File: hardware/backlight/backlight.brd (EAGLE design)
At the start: 58.4 x 68.2 mm, 39 parts, among them J1 1x8 header, U1 ATTINY45-20SU

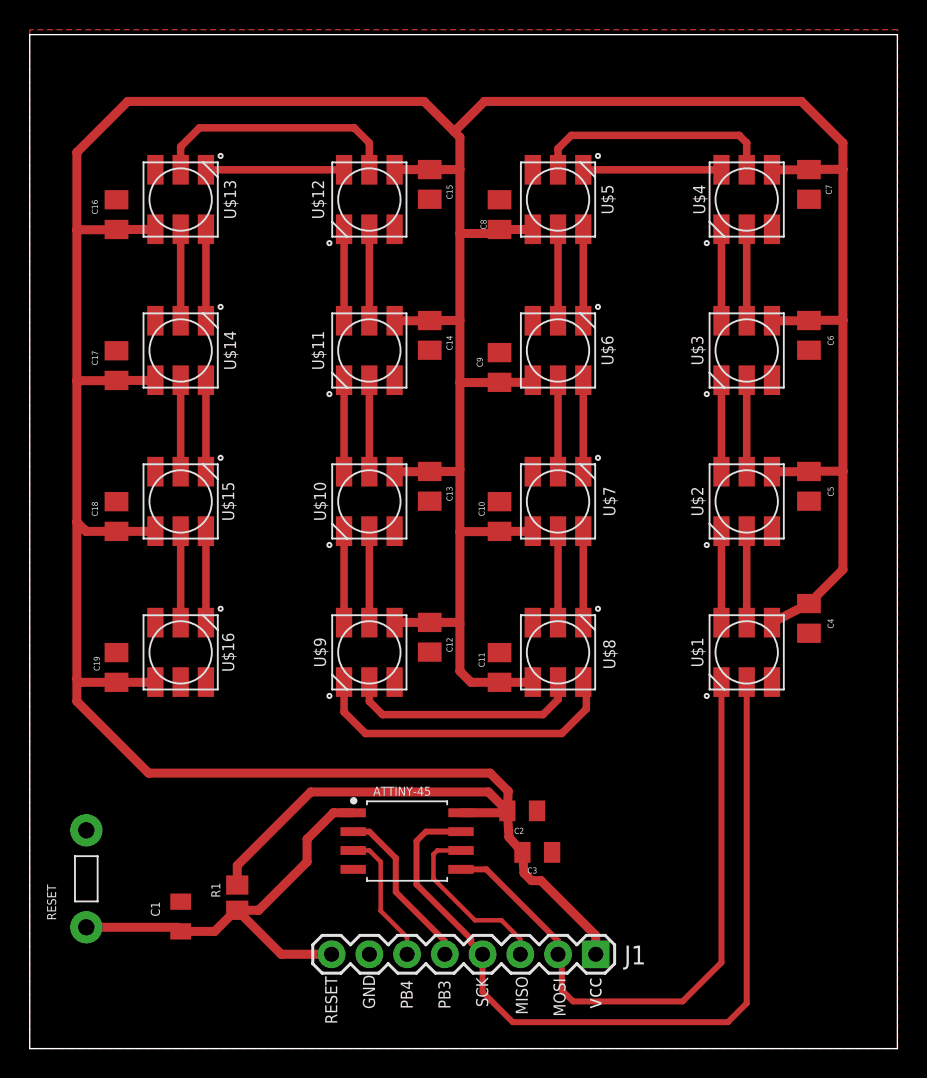
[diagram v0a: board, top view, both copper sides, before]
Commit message: thicken traces again
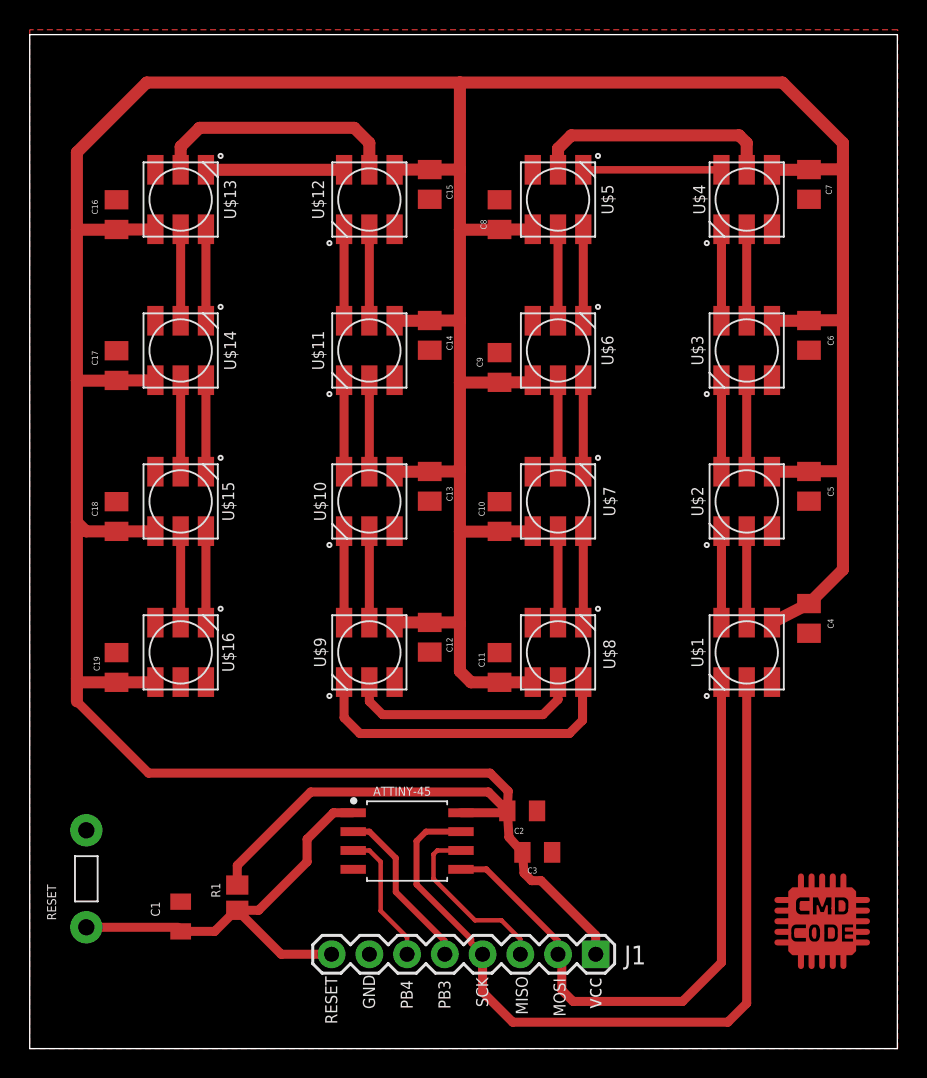
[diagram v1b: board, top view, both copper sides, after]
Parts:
- added U$17: CMD_C0DE_LOGOCMD_CODE_LOGO_TOP_COPPER, logos:CMD_C0DE_LOGO_TOP_COPPER
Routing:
- net VCC: track 308.3 -> 310.7 mm
